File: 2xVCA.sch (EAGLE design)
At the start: 50 parts, among them IC1 TL072P, IC2 LM13700N, IC3 TL072P, Q1 2N3906, Q2 2N3906, Q3 BC548B, Q4 BC548B

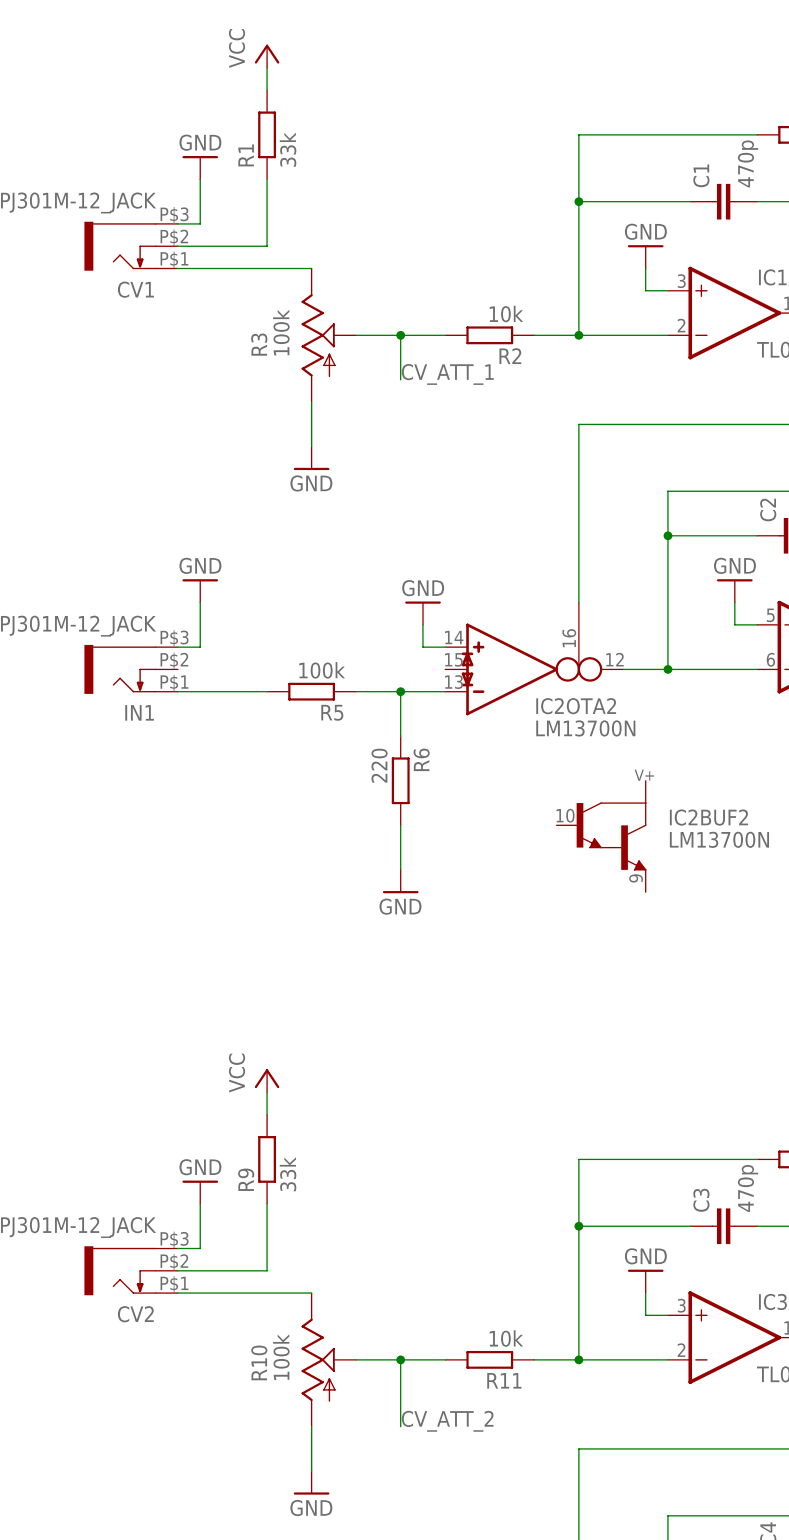
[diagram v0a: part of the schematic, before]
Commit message: Updated component values for use with 10k potentiometers.
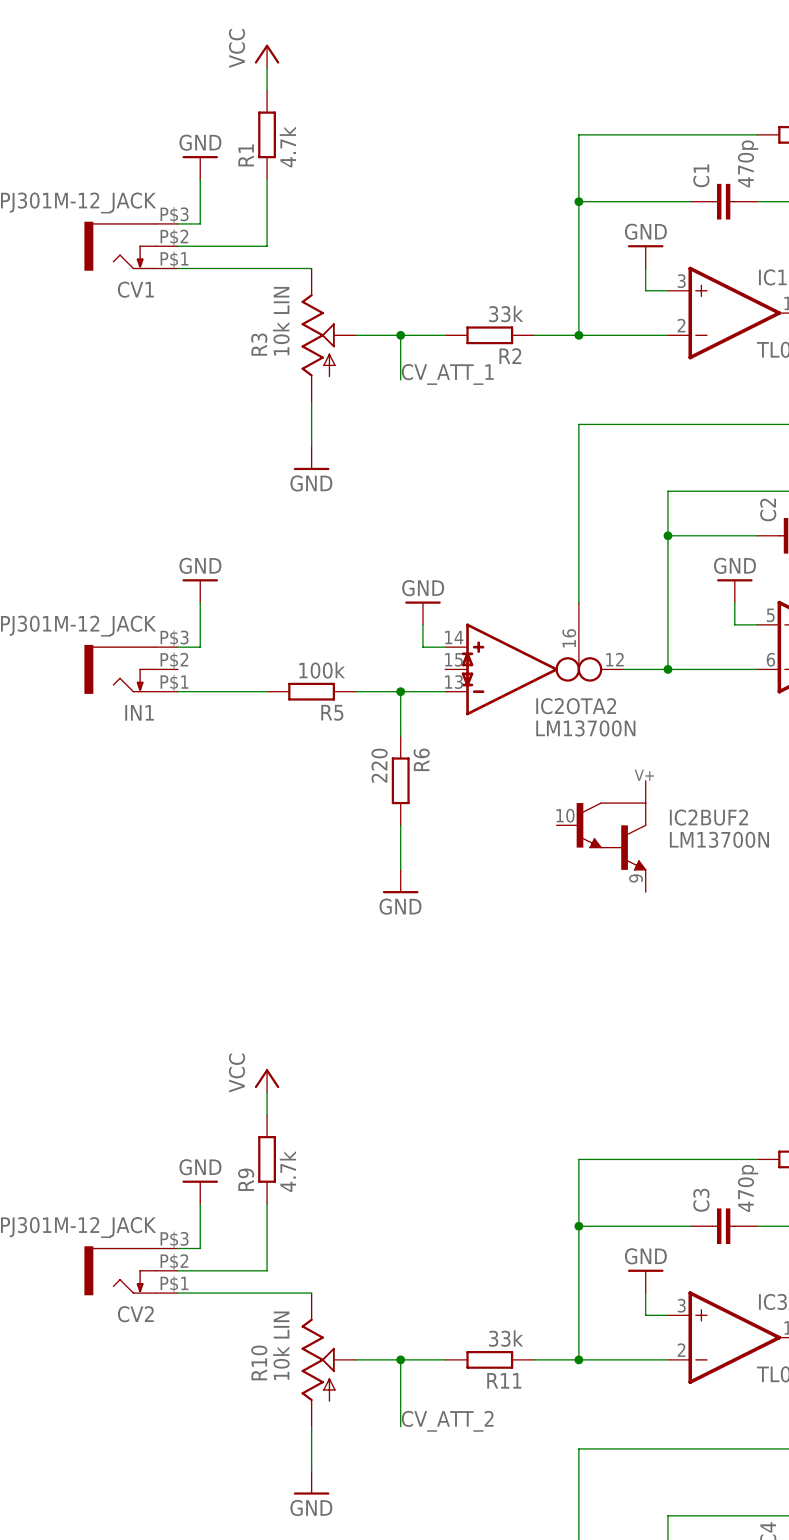
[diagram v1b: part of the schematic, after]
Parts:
- R1, R9: value 33k -> 4.7k
- R10, R3: value 100k -> 10k LIN
- R11, R2: value 10k -> 33k
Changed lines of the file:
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@@
 <part name="FRAME1" library="frames" deviceset="DINA3_L" device=""/>
 <part name="CV1" library="thonkiconn" deviceset="WQP-PJ301M-12_JACK" device=""/>
-<part name="R1" library="rcl" deviceset="R-EU_" device="0207/2V" value="33k"/>
-<part name="R2" library="rcl" deviceset="R-EU_" device="0207/2V" value="10k"/>
-<part name="R3" library="pot-alps" deviceset="POT_US" device="VERTICAL" value="100k"/>
+<part name="R1" library="rcl" deviceset="R-EU_" device="0207/2V" value="4.7k"/>
+<part name="R2" library="rcl" deviceset="R-EU_" device="0207/2V" value="33k"/>
+<part name="R3" library="pot-alps" deviceset="POT_US" device="VERTICAL" value="10k LIN"/>
 <part name="IC1" library="linear" deviceset="TL072" device="P"/>
 <part name="GND1" library="supply1" deviceset="GND" device=""/>
@@
 <part name="CV2" library="thonkiconn" deviceset="WQP-PJ301M-12_JACK" device=""/>
 <part name="GND9" library="supply1" deviceset="GND" device=""/>
-<part name="R9" library="rcl" deviceset="R-EU_" device="0207/2V" value="33k"/>
-<part name="R10" library="pot-alps" deviceset="POT_US" device="VERTICAL" value="100k"/>
+<part name="R9" library="rcl" deviceset="R-EU_" device="0207/2V" value="4.7k"/>
+<part name="R10" library="pot-alps" deviceset="POT_US" device="VERTICAL" value="10k LIN"/>
 <part name="P+2" library="supply1" deviceset="VCC" device=""/>
 <part name="GND10" library="supply1" deviceset="GND" device=""/>
-<part name="R11" library="rcl" deviceset="R-EU_" device="0207/2V" value="10k"/>
+<part name="R11" library="rcl" deviceset="R-EU_" device="0207/2V" value="33k"/>
 <part name="IC3" library="linear" deviceset="TL072" device="P"/>
 <part name="C3" library="rcl" deviceset="C-EU" device="025-025X050" value="470p"/>
